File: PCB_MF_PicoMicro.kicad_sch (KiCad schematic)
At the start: 5 parts, among them J7 Conn_01x02_Pin, J8 Conn_01x02_Pin, U5 ProMicro

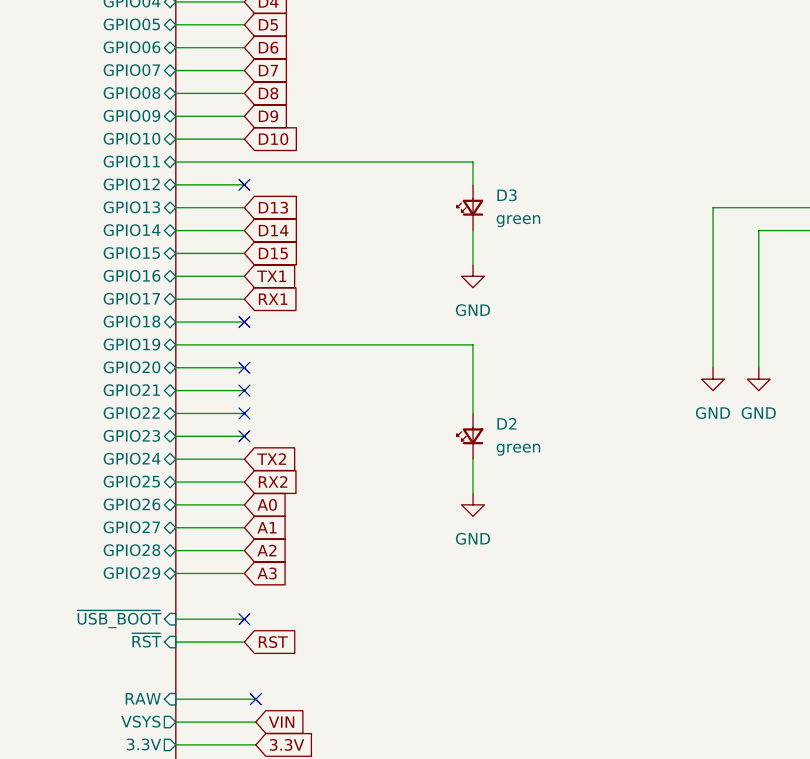
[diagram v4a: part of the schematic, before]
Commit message: add missing R for LEDs, add production files for JLCPCB
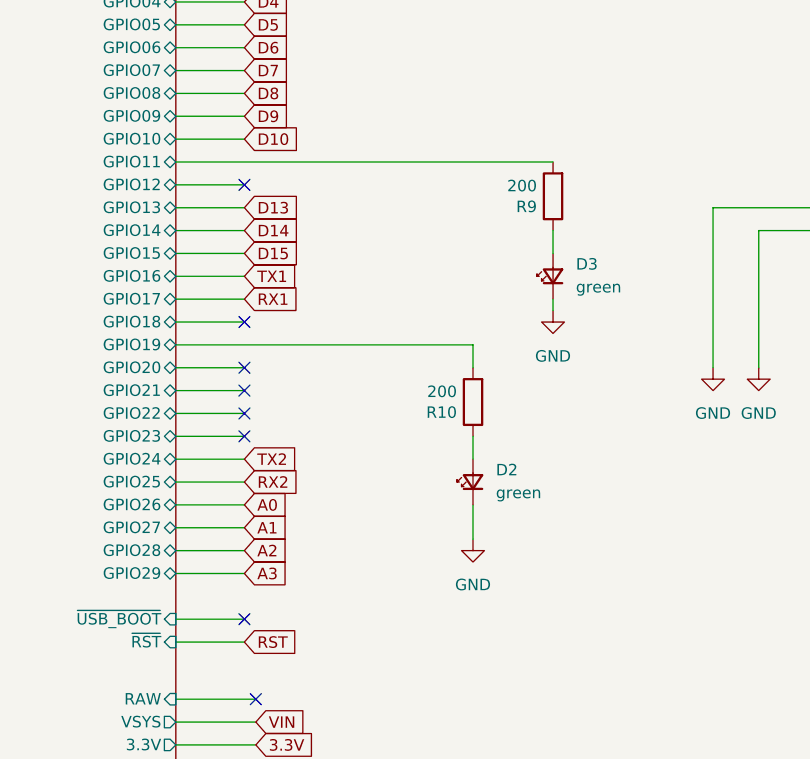
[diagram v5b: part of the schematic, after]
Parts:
- added R10, R9: 200, Resistor_SMD:R_0402_1005Metric, symbol Device:R
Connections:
- net RP2350A/GPIO11: now also R9.2; no longer D3.2 (A)
- net RP2350A/GPIO19: now also R10.2; no longer D2.2 (A)
- new net: D3.2 (A), R9.1
- new net: D2.2 (A), R10.1
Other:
- moved on the sheet: D2, D3
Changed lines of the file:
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@@
 	(wire
 		(pts
-			(xy 81.28 97.79) (xy 81.28 101.6)
+			(xy 81.28 102.87) (xy 81.28 106.68)
 		)
 		(stroke
@@
 	(wire
 		(pts
+			(xy 81.28 95.25) (xy 81.28 97.79)
+		)
+		(stroke
+			(width 0)
+			(type default)
+		)
+	)
+	(wire
+		(pts
 			(xy 177.8 69.85) (xy 182.88 69.85)
 		)
@@
 	(wire
 		(pts
-			(xy 81.28 64.77) (xy 81.28 67.31)
+			(xy 81.28 85.09) (xy 81.28 87.63)
 		)
 		(stroke
@@
 	(wire
 		(pts
-			(xy 81.28 85.09) (xy 81.28 92.71)
-		)
-		(stroke
-			(width 0)
-			(type default)
-		)
-	)
-	(wire
-		(pts
 			(xy 48.26 41.91) (xy 55.88 41.91)
 		)
@@
 	(wire
 		(pts
-			(xy 48.26 64.77) (xy 81.28 64.77)
+			(xy 48.26 64.77) (xy 90.17 64.77)
 		)
 		(stroke
@@
 	(wire
 		(pts
+			(xy 90.17 72.39) (xy 90.17 74.93)
+		)
+		(stroke
+			(width 0)
+			(type default)
+		)
+	)
+	(wire
+		(pts
 			(xy 48.26 85.09) (xy 81.28 85.09)
 		)
@@
 	(wire
 		(pts
-			(xy 81.28 72.39) (xy 81.28 76.2)
+			(xy 90.17 80.01) (xy 90.17 81.28)
 		)
 		(stroke
@@
 	)
 	(symbol
-		(lib_id "power:GND")
-		(at 81.28 101.6 0)
+		(lib_id "Device:R")
+		(at 90.17 68.58 180)
 		(unit 1)
 		(exclude_from_sim no)
@@
 		(on_board yes)
 		(dnp no)
+		(property "Reference" "R9"
+			(at 88.392 69.7484 0)
+			(effects
+				(font
+					(size 1.27 1.27)
+				)
+				(justify left)
+			)
+		)
+		(property "Value" "200"
+			(at 88.392 67.437 0)
+			(effects
+				(font
+					(size 1.27 1.27)
+				)
+				(justify left)
+			)
+		)
+		(property "Footprint" "Resistor_SMD:R_0402_1005Metric"
+			(at 91.948 68.58 90)
+			(effects
+				(font
+					(size 1.27 1.27)
+				)
+				(hide yes)
+			)
+		)
+		(property "Datasheet" "~"
+			(at 90.17 68.58 0)
+			(effects
+				(font
+					(size 1.27 1.27)
+				)
+				(hide yes)
+			)
+		)
+		(property "Description" ""
+			(at 90.17 68.58 0)
+			(effects
+				(font
+					(size 1.27 1.27)
+				)
+			)
+		)
+		(pin "1"
+		)
+		(pin "2"
+		)
+		(instances
+			(project "PCB_MF_PicoMicro"
+				(path "/e63e39d7-6ac0-4ffd-8aa3-1841a4541b55"
+					(reference "R9")
+					(unit 1)
+				)
+			)
+		)
+	)
+	(symbol
+		(lib_id "power:GND")
+		(at 81.28 106.68 0)
+		(unit 1)
+		(exclude_from_sim no)
+		(in_bom yes)
+		(on_board yes)
+		(dnp no)
 		(fields_autoplaced yes)
 		(property "Reference" "#PWR017"
-			(at 81.28 107.95 0)
+			(at 81.28 113.03 0)
 			(effects
 				(font
@@
 		)
 		(property "Value" "GND"
+			(at 81.28 111.76 0)
+			(effects
+				(font
+					(size 1.27 1.27)
+				)
+			)
+		)
+		(property "Footprint" ""
 			(at 81.28 106.68 0)
 			(effects
@@
 					(size 1.27 1.27)
 				)
-			)
-		)
-		(property "Footprint" ""
-			(at 81.28 101.6 0)
-			(effects
-				(font
-					(size 1.27 1.27)
-				)
 				(hide yes)
 			)
 		)
 		(property "Datasheet" ""
-			(at 81.28 101.6 0)
+			(at 81.28 106.68 0)
 			(effects
 				(font
@@
 		)
 		(property "Description" "Power symbol creates a global label with name \"GND\" , ground"
-			(at 81.28 101.6 0)
+			(at 81.28 106.68 0)
 			(effects
 				(font
@@
 	(symbol
 		(lib_id "Device:LED_Small")
-		(at 81.28 95.25 90)
+		(at 81.28 100.33 90)
 		(unit 1)
 		(exclude_from_sim no)
@@
 		(fields_autoplaced yes)
 		(property "Reference" "D2"
-			(at 83.82 93.9164 90)
+			(at 83.82 98.9964 90)
 			(effects
 				(font
@@
 		)
 		(property "Value" "green"
-			(at 83.82 96.4564 90)
+			(at 83.82 101.5364 90)
 			(effects
 				(font
@@
 		)
 		(property "Footprint" "LED_SMD:LED_0402_1005Metric"
-			(at 81.28 95.25 90)
+			(at 81.28 100.33 90)
 			(effects
 				(font
@@
 		)
 		(property "Datasheet" "~"
-			(at 81.28 95.25 90)
+			(at 81.28 100.33 90)
 			(effects
 				(font
@@
 		)
 		(property "Description" "Light emitting diode, small symbol"
-			(at 81.28 95.25 0)
+			(at 81.28 100.33 0)
 			(effects
 				(font
@@
 		)
 		(property "Sim.Pin" "1=K 2=A"
-			(at 81.28 95.25 0)
+			(at 81.28 100.33 0)
 			(effects
 				(font
@@
 	)
 	(symbol
-		(lib_id "Device:LED_Small")
-		(at 81.28 69.85 90)
+		(lib_id "Device:R")
+		(at 81.28 91.44 180)
 		(unit 1)
 		(exclude_from_sim no)
@@
 		(on_board yes)
 		(dnp no)
+		(property "Reference" "R10"
+			(at 79.502 92.6084 0)
+			(effects
+				(font
+					(size 1.27 1.27)
+				)
+				(justify left)
+			)
+		)
+		(property "Value" "200"
+			(at 79.502 90.297 0)
+			(effects
+				(font
+					(size 1.27 1.27)
+				)
+				(justify left)
+			)
+		)
+		(property "Footprint" "Resistor_SMD:R_0402_1005Metric"
+			(at 83.058 91.44 90)
+			(effects
+				(font
+					(size 1.27 1.27)
+				)
+				(hide yes)
+			)
+		)
+		(property "Datasheet" "~"
+			(at 81.28 91.44 0)
+			(effects
+				(font
+					(size 1.27 1.27)
+				)
+				(hide yes)
+			)
+		)
+		(property "Description" ""
+			(at 81.28 91.44 0)
+			(effects
+				(font
+					(size 1.27 1.27)
+				)
+			)
+		)
+		(pin "1"
+		)
+		(pin "2"
+		)
+		(instances
+			(project "PCB_MF_PicoMicro"
+				(path "/e63e39d7-6ac0-4ffd-8aa3-1841a4541b55"
+					(reference "R10")
+					(unit 1)
+				)
+			)
+		)
+	)
+	(symbol
+		(lib_id "Device:LED_Small")
+		(at 90.17 77.47 90)
+		(unit 1)
+		(exclude_from_sim no)
+		(in_bom yes)
+		(on_board yes)
+		(dnp no)
 		(fields_autoplaced yes)
 		(property "Reference" "D3"
-			(at 83.82 68.5164 90)
+			(at 92.71 76.1364 90)
 			(effects
 				(font
@@
 		)
 		(property "Value" "green"
-			(at 83.82 71.0564 90)
+			(at 92.71 78.6764 90)
 			(effects
 				(font
@@
 		)
 		(property "Footprint" "LED_SMD:LED_0402_1005Metric"
-			(at 81.28 69.85 90)
+			(at 90.17 77.47 90)
 			(effects
 				(font
@@
 		)
 		(property "Datasheet" "~"
-			(at 81.28 69.85 90)
+			(at 90.17 77.47 90)
 			(effects
 				(font
@@
 		)
 		(property "Description" "Light emitting diode, small symbol"
-			(at 81.28 69.85 0)
+			(at 90.17 77.47 0)
 			(effects
 				(font
@@
 		)
 		(property "Sim.Pin" "1=K 2=A"
-			(at 81.28 69.85 0)
+			(at 90.17 77.47 0)
 			(effects
 				(font
@@
 	(symbol
 		(lib_id "power:GND")
-		(at 81.28 76.2 0)
+		(at 90.17 81.28 0)
 		(unit 1)
 		(exclude_from_sim no)
@@
 		(fields_autoplaced yes)
 		(property "Reference" "#PWR018"
-			(at 81.28 82.55 0)
+			(at 90.17 87.63 0)
 			(effects
 				(font
@@
 		)
 		(property "Value" "GND"
-			(at 81.28 81.28 0)
+			(at 90.17 86.36 0)
 			(effects
 				(font
@@
 		)
 		(property "Footprint" ""
-			(at 81.28 76.2 0)
+			(at 90.17 81.28 0)
 			(effects
 				(font
@@
 		)
 		(property "Datasheet" ""
-			(at 81.28 76.2 0)
+			(at 90.17 81.28 0)
 			(effects
 				(font
@@
 		)
 		(property "Description" "Power symbol creates a global label with name \"GND\" , ground"
-			(at 81.28 76.2 0)
-			(effects
-				(font
+			(at 90.17 81.28 0)
+			(effects
+				(font

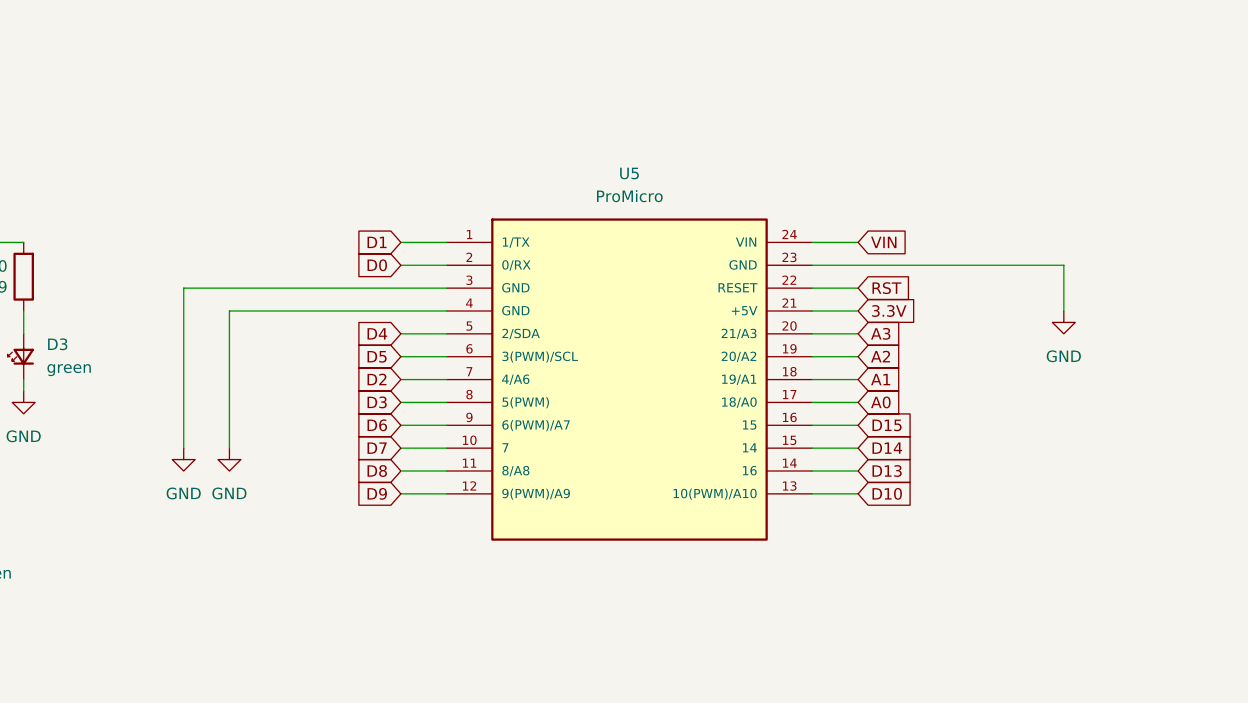
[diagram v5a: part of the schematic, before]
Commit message: replace ProMicro against pin header connectors
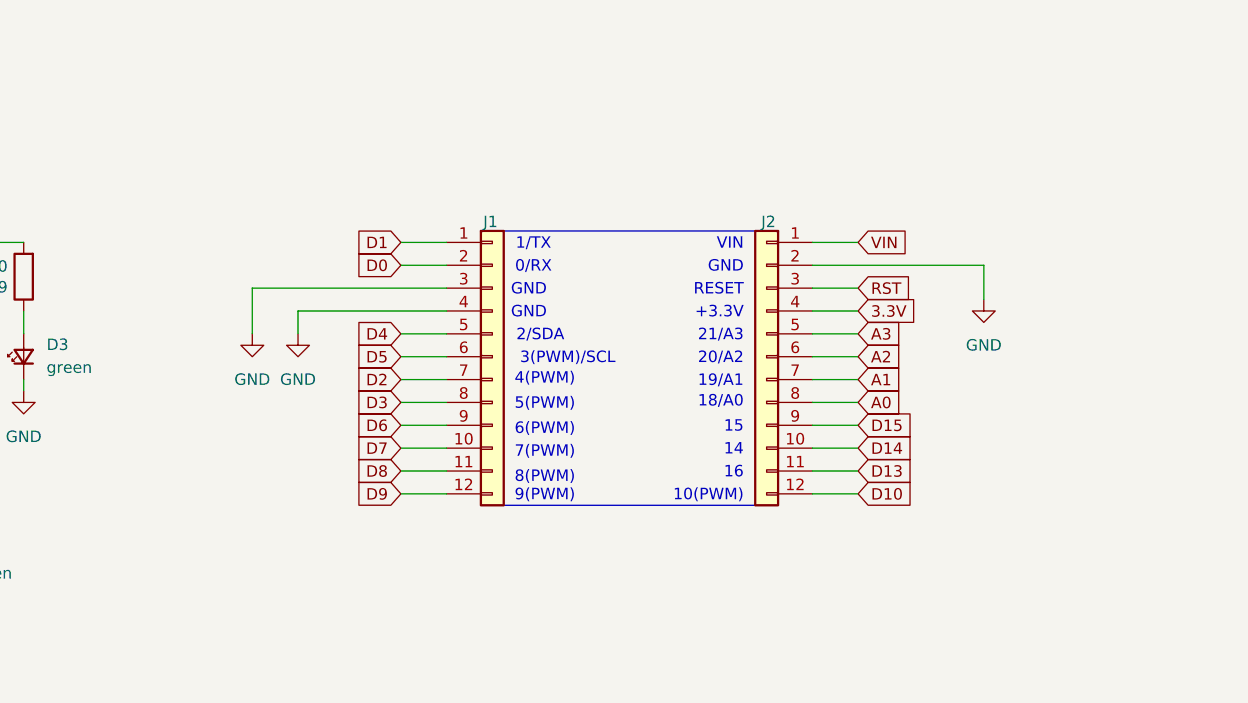
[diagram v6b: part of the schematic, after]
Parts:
- removed U5: ProMicro, _Own_Library:ProMicro, symbol Own_Library:PoMicro
- added J1, J2: Conn_01x12, Connector_PinHeader_2.54mm:PinHeader_1x12_P2.54mm_Vertical, symbol Connector_Generic:Conn_01x12
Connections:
- net 3.3V: now also J2.4 (Pin_4)
- net A0: now also J2.8 (Pin_8)
- net A1: now also J2.7 (Pin_7)
- net A2: now also J2.6 (Pin_6)
- net A3: now also J2.5 (Pin_5)
- net D0: now also J1.2 (Pin_2)
- net D1: now also J1.1 (Pin_1)
- net D10: now also J2.12 (Pin_12)
- net D13: now also J2.11 (Pin_11)
- net D14: now also J2.10 (Pin_10)
- net D15: now also J2.9 (Pin_9)
- net D2: now also J1.7 (Pin_7)
- net D3: now also J1.8 (Pin_8)
- net D4: now also J1.5 (Pin_5)
- net D5: now also J1.6 (Pin_6)
- net D6: now also J1.9 (Pin_9)
- net D7: now also J1.10 (Pin_10)
- net D8: now also J1.11 (Pin_11)
- net D9: now also J1.12 (Pin_12)
- net GND: now also J1.3 (Pin_3), J1.4 (Pin_4), J2.2 (Pin_2)
- net RST: now also J2.3 (Pin_3)
- net VIN: now also J2.1 (Pin_1)
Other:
- note added: "+3.3V"
- note added: "0/RX"
- note added: "1/TX"
- note added: "10(PWM)"
- note added: "14"
- note added: "15"
- note added: "16"
- note added: "18/A0"
- note added: "19/A1"
- note added: "2/SDA"
- note added: "20/A2"
- note added: "21/A3"
- note added: "3(PWM)/SCL"
- note added: "4(PWM)"
- note added: "5(PWM)"
- note added: "6(PWM)"
- note added: "7(PWM)"
- note added: "8(PWM)"
- note added: "9(PWM)"
- note added: "GND"
- note added: "RESET"
- note added: "VIN"
